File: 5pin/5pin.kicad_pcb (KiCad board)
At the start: 2 copper layers, 14 x 20 mm, 2 parts, among them J1 B05B-PASK-1(LF)(SN), J2 UR01-07-5

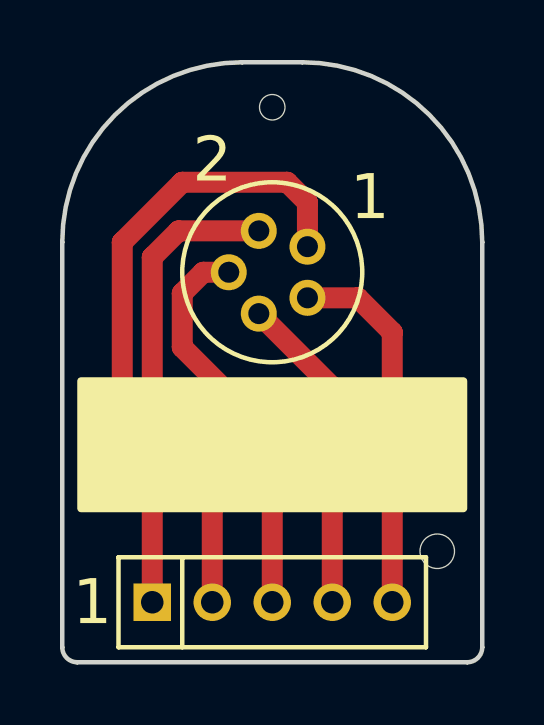
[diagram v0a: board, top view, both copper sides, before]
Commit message: Change design and foot print of the 5 pin, fabrication 3 pins near done
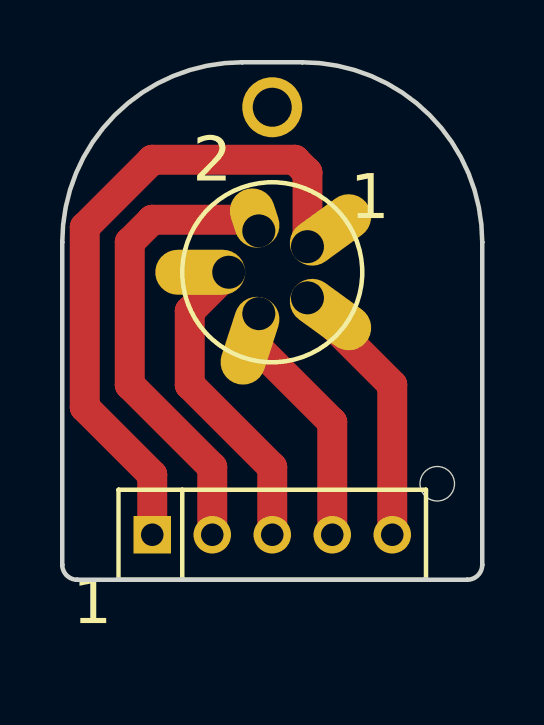
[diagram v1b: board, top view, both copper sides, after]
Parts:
- J2: value UR01-07-5 -> CPA_5
- moved J1 2.25 mm to (150.0, 108.8)
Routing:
- net Net-(J1-Pad5): track 12.3 -> 9.07 mm
- net Net-(J1-Pad3): track 13.4 -> 10.4 mm
- net Net-(J1-Pad4): track 10.6 -> 8.38 mm
- net Net-(J1-Pad1): track 21.2 -> 22.2 mm
- net Net-(J1-Pad2): track 16.2 -> 15.7 mm
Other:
- board size 14 x 20 mm -> 14 x 17.2 mm
- net class Default: trace_width 0.7 -> 1
- rule pad_to_mask_clearance: 0.2 -> 0.05

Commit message: change in Layout
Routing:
- net Net-(J1-Pad1): track 22.2 -> 12.5 mm
- net Net-(J1-Pad5): track 9.07 -> 17.2 mm
- net Net-(J1-Pad2): track 15.7 -> 8.24 mm
- net Net-(J1-Pad3): track 10.4 -> 7.56 mm
- net Net-(J1-Pad4): track 8.38 -> 9.84 mm
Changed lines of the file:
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@@
     (thickness 1.6)
     (drawings 13)
-    (tracks 23)
+    (tracks 20)
     (zones 0)
     (modules 2)
@@
     (add_net "Net-(J1-Pad5)")
   )
+  (module fisher:UR01-07-5 (layer F.Cu)
+    (at 150 100)
+    (fp_text reference J2 (at 0 -3.025) (layer F.SilkS) hide
+      (effects (font (size 1.2 1.2) (thickness 0.15)))
+    )
+    (fp_text value CPA_5 (at 0 3.025) (layer F.Fab) hide
+      (effects (font (size 1.2 1.2) (thickness 0.15)))
+    )
+    (fp_circle (center 0 0) (end 0 3) (layer F.SilkS) (width 0.15))
+    (fp_circle (center 0 0) (end 0 7) (layer F.CrtYd) (width 0.15))
+    (pad "" thru_hole circle (at 0 -5.5) (size 2 2) (drill 1.3) (layers *.Cu *.Mask))
+    (pad 2 thru_hole oval (at -1.173074 0.852288 216) (size 3 1.5) (drill 1.3 (offset 0.85 0)) (layers *.Cu *.Mask)
+      (net 2 "Net-(J1-Pad2)"))
+    (pad 3 thru_hole oval (at 0.448074 1.379031 288) (size 3 1.5) (drill 1.3 (offset 0.85 0)) (layers *.Cu *.Mask)
+      (net 3 "Net-(J1-Pad3)"))
+    (pad 4 thru_hole oval (at 1.45 0) (size 3 1.5) (drill 1.3 (offset 0.85 0)) (layers *.Cu *.Mask)
+      (net 4 "Net-(J1-Pad4)"))
+    (pad 5 thru_hole oval (at 0.448074 -1.379031 72) (size 3 1.5) (drill 1.3 (offset 0.85 0)) (layers *.Cu *.Mask)
+      (net 5 "Net-(J1-Pad5)"))
+    (pad 1 thru_hole oval (at -1.173074 -0.852288 144) (size 3 1.5) (drill 1.3 (offset 0.85 0)) (layers *.Cu *.Mask)
+      (net 1 "Net-(J1-Pad1)"))
+  )
   (module "jsetpa: B05B-PASK-1(LF)(SN)" (layer F.Cu)
     (at 150 108.75)
@@
       (net 1 "Net-(J1-Pad1)"))
   )
-  (module fisher:UR01-07-5 (layer F.Cu)
-    (at 150 100)
-    (fp_text reference J2 (at 0 -3.025) (layer F.SilkS) hide
-      (effects (font (size 1.2 1.2) (thickness 0.15)))
-    )
-    (fp_text value CPA_5 (at 0 3.025) (layer F.Fab) hide
-      (effects (font (size 1.2 1.2) (thickness 0.15)))
-    )
-    (fp_circle (center 0 0) (end 0 3) (layer F.SilkS) (width 0.15))
-    (fp_circle (center 0 0) (end 0 7) (layer F.CrtYd) (width 0.15))
-    (pad "" thru_hole circle (at 0 -5.5) (size 2 2) (drill 1.3) (layers *.Cu *.Mask))
-    (pad 5 thru_hole oval (at 1.173074 0.852288 144) (size 3 1.5) (drill 1.1 (offset -0.95 0)) (layers *.Cu *.Mask)
-      (net 5 "Net-(J1-Pad5)"))
-    (pad 4 thru_hole oval (at -0.448074 1.379031 72) (size 3 1.5) (drill 1.1 (offset -0.95 0)) (layers *.Cu *.Mask)
-      (net 4 "Net-(J1-Pad4)"))
-    (pad 3 thru_hole oval (at -1.45 0) (size 3 1.5) (drill 1.1 (offset -0.95 0)) (layers *.Cu *.Mask)
-      (net 3 "Net-(J1-Pad3)"))
-    (pad 2 thru_hole oval (at -0.448074 -1.379031 288) (size 2 1.5) (drill 1.1 (offset -0.45 0)) (layers *.Cu *.Mask)
-      (net 2 "Net-(J1-Pad2)"))
-    (pad 1 thru_hole oval (at 1.173074 -0.852288 216) (size 3 1.5) (drill 1.1 (offset -0.95 0)) (layers *.Cu *.Mask)
-      (net 1 "Net-(J1-Pad1)"))
-  )
   (dimension 17.25 (width 0.3) (layer Cmts.User)
     (gr_text "17.250 mm" (at 160.35 101.625 90) (layer Cmts.User)
@@
     (effects (font (size 1.5 1.5) (thickness 0.3)))
   )
-  (segment (start 151.173074 99.147712) (end 151.173074 96.673074) (width 1) (layer F.Cu) (net 1))
-  (segment (start 151.173074 96.673074) (end 150.75 96.25) (width 1) (layer F.Cu) (net 1))
-  (segment (start 150.75 96.25) (end 146 96.25) (width 1) (layer F.Cu) (net 1))
-  (segment (start 146 96.25) (end 143.75 98.5) (width 1) (layer F.Cu) (net 1))
-  (segment (start 143.75 98.5) (end 143.75 104.5) (width 1) (layer F.Cu) (net 1))
-  (segment (start 143.75 104.5) (end 146 106.75) (width 1) (layer F.Cu) (net 1))
-  (segment (start 146 106.75) (end 146 108.75) (width 1) (layer F.Cu) (net 1))
-  (segment (start 149.180957 98.25) (end 149.551926 98.620969) (width 0.7) (layer F.Cu) (net 2))
-  (segment (start 146 98.25) (end 149.180957 98.25) (width 1) (layer F.Cu) (net 2))
-  (segment (start 145.25 99) (end 146 98.25) (width 1) (layer F.Cu) (net 2))
-  (segment (start 145.25 103.75) (end 145.25 99) (width 1) (layer F.Cu) (net 2))
-  (segment (start 148 106.5) (end 145.25 103.75) (width 1) (layer F.Cu) (net 2))
-  (segment (start 148 106.5) (end 148 108.75) (width 1) (layer F.Cu) (net 2))
-  (segment (start 148.55 100) (end 147.25 101.3) (width 1) (layer F.Cu) (net 3))
-  (segment (start 147.25 101.3) (end 147.25 103.75) (width 1) (layer F.Cu) (net 3))
-  (segment (start 147.25 103.75) (end 150 106.5) (width 1) (layer F.Cu) (net 3))
-  (segment (start 150 106.5) (end 150 108.75) (width 1) (layer F.Cu) (net 3))
-  (segment (start 149.551926 101.379031) (end 149.551926 102.551926) (width 0.7) (layer F.Cu) (net 4))
-  (segment (start 149.551926 102.551926) (end 152 105) (width 1) (layer F.Cu) (net 4))
-  (segment (start 152 105) (end 152 108.75) (width 1) (layer F.Cu) (net 4))
-  (segment (start 151.173074 100.852288) (end 151.173074 100.923074) (width 0.7) (layer F.Cu) (net 5))
-  (segment (start 151.173074 100.923074) (end 154 103.75) (width 1) (layer F.Cu) (net 5))
-  (segment (start 154 103.75) (end 154 108.75) (width 1) (layer F.Cu) (net 5))
+  (segment (start 148.127067 99.147712) (end 148.039355 99.06) (width 1) (layer F.Cu) (net 1))
+  (segment (start 148.826926 99.147712) (end 148.127067 99.147712) (width 1) (layer F.Cu) (net 1))
+  (segment (start 146 100.38) (end 146 108.75) (width 1) (layer F.Cu) (net 1))
+  (segment (start 147.232288 99.147712) (end 146 100.38) (width 1) (layer F.Cu) (net 1))
+  (segment (start 148.826926 99.147712) (end 147.232288 99.147712) (width 1) (layer F.Cu) (net 1))
+  (segment (start 148 101.679214) (end 148.826926 100.852288) (width 1) (layer F.Cu) (net 2))
+  (segment (start 148 108.75) (end 148 101.679214) (width 1) (layer F.Cu) (net 2))
+  (segment (start 150.448074 101.379031) (end 150.448074 102.281926) (width 1) (layer F.Cu) (net 3))
+  (segment (start 150 102.73) (end 150 108.75) (width 1) (layer F.Cu) (net 3))
+  (segment (start 150.448074 102.281926) (end 150 102.73) (width 1) (layer F.Cu) (net 3))
+  (segment (start 152 108.75) (end 152 105.175) (width 1) (layer F.Cu) (net 4))
+  (segment (start 152 105.175) (end 153.035 104.14) (width 1) (layer F.Cu) (net 4))
+  (segment (start 153.035 101.585) (end 151.45 100) (width 1) (layer F.Cu) (net 4))
+  (segment (start 153.035 104.14) (end 153.035 101.585) (width 1) (layer F.Cu) (net 4))
+  (segment (start 154 108.75) (end 154 105.74) (width 1) (layer F.Cu) (net 5))
+  (segment (start 154 105.74) (end 155.575 104.165) (width 1) (layer F.Cu) (net 5))
+  (segment (start 155.575 104.165) (end 155.575 98.425) (width 1) (layer F.Cu) (net 5))
+  (segment (start 155.575 98.425) (end 154.305 97.155) (width 1) (layer F.Cu) (net 5))
+  (segment (start 151.914043 97.155) (end 150.448074 98.620969) (width 1) (layer F.Cu) (net 5))
+  (segment (start 154.305 97.155) (end 151.914043 97.155) (width 1) (layer F.Cu) (net 5))
 )
